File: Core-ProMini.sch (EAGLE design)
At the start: 28 parts, among them CON1 5.08, CON2 2mm, CON3 0.100, IC1 cj7805, J2 IO4, J4 2.1mm, J5 IO4, J6 IO4, J7 IO4

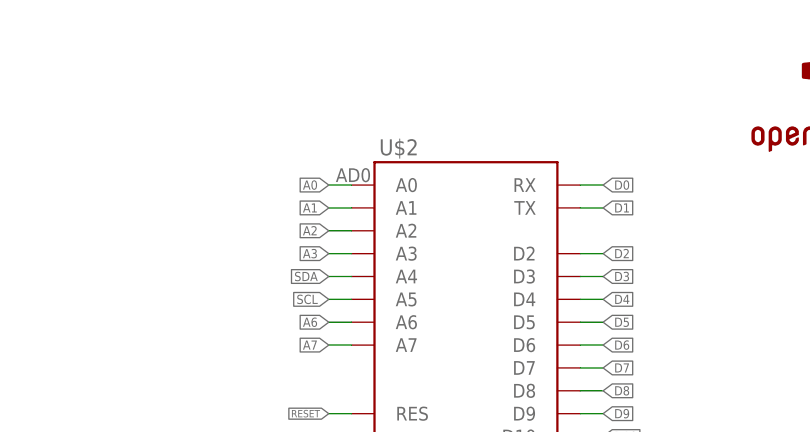
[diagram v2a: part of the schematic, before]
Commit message: updated part names
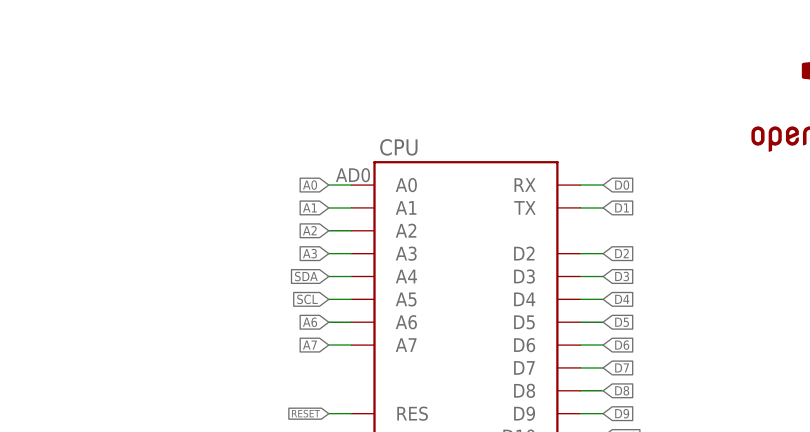
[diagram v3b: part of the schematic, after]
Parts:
- OSH: value DOC-OSHW-LOGO-L -> L
- renumbered LOGO1 to OSH, U$2 to CPU, U$3 to PWR, U$4 to BOARD
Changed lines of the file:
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@@
 <part name="V1" library="supply2" deviceset="GND" device=""/>
 <part name="C5" library="SPCoast" deviceset="CAP-POL*" device="0810" value="150uF"/>
-<part name="U$2" library="SPCoast" deviceset="ARDUINO-PRO-MINI" device="DAVESROBOT"/>
+<part name="CPU" library="SPCoast" deviceset="ARDUINO-PRO-MINI" device="DAVESROBOT"/>
 <part name="J4" library="SPCoast" deviceset="CONNECTOR-DC-POWER" device="-RA" value="2.1mm"/>
-<part name="U$3" library="SPCoast" deviceset="DOC-POWER_LABEL" device="" value="9-12vDC"/>
+<part name="PWR" library="SPCoast" deviceset="DOC-POWER_LABEL" device="" value="9-12vDC"/>
 <part name="VCC12" library="supply1" deviceset="VCCIO" device=""/>
 <part name="V15" library="supply2" deviceset="GND" device=""/>
 <part name="VCC13" library="supply1" deviceset="VCCIO" device=""/>
-<part name="U$4" library="SPCoast" deviceset="BOARD" device="69X100MRCS" value="BOARD69X100MRCS"/>
+<part name="BOARD" library="SPCoast" deviceset="BOARD" device="69X100MRCS" value="BOARD69X100MRCS"/>
 <part name="C1" library="SPCoast" deviceset="CAP*" device="0805" value="1uF"/>
 <part name="C2" library="SPCoast" deviceset="CAP*" device="0805" value="1uF"/>
-<part name="LOGO1" library="SPCoast" deviceset="DOC-OSHW-LOGO-" device="L"/>
+<part name="OSH" library="SPCoast" deviceset="DOC-OSHW-LOGO-" device="L" value="L"/>
 <part name="IC1" library="SPCoast" deviceset="VREG-?-*" device="DPAK" technology="5" value="cj7805"/>
 <part name="CON1" library="SPCoast" deviceset="CONNECTOR-M02" device="508-LOCK" value="5.08"/>
@@
 <instance part="V1" gate="GND" x="160.02" y="68.58" rot="R270"/>
 <instance part="C5" gate="C1" x="175.26" y="96.52"/>
-<instance part="U$2" gate="A" x="190.5" y="144.78"/>
+<instance part="CPU" gate="A" x="190.5" y="144.78"/>
 <instance part="J4" gate="J" x="157.48" y="99.06"/>
-<instance part="U$3" gate="PWR1" x="157.48" y="109.22"/>
+<instance part="PWR" gate="PWR1" x="157.48" y="109.22"/>
 <instance part="VCC12" gate="G$1" x="205.74" y="68.58"/>
 <instance part="V15" gate="GND" x="175.26" y="121.92"/>
 <instance part="VCC13" gate="G$1" x="170.18" y="129.54"/>
-<instance part="U$4" gate="B" x="236.22" y="40.64"/>
+<instance part="BOARD" gate="B" x="236.22" y="40.64"/>
 <instance part="C1" gate="C1" x="203.2" y="96.52" smashed="yes">
 <attribute name="NAME" x="198.501" y="100.076" size="1.778" layer="95" rot="R270"/>
@@
 <attribute name="VALUE" x="184.531" y="95.758" size="1.016" layer="96" rot="R270"/>
 </instance>
-<instance part="LOGO1" gate="DOC-OSHW-LOGO" x="233.68" y="55.88"/>
+<instance part="OSH" gate="DOC-OSHW-LOGO" x="233.68" y="55.88"/>
 <instance part="IC1" gate="VR" x="193.04" y="101.6"/>
 <instance part="CON1" gate="J" x="220.98" y="81.28" rot="MR180"/>
@@
 </segment>
 <segment>
-<pinref part="U$2" gate="A" pin="GND"/>
+<pinref part="CPU" gate="A" pin="GND"/>
 <wire x1="177.8" y1="124.46" x2="175.26" y2="124.46" width="0.1524" layer="91"/>
 <pinref part="V15" gate="GND" pin="GND"/>
@@
 <wire x1="205.74" y1="165.1" x2="203.2" y2="165.1" width="0.1524" layer="91"/>
 <label x="205.74" y="165.1" size="1.016" layer="95" xref="yes"/>
-<pinref part="U$2" gate="A" pin="RX"/>
+<pinref part="CPU" gate="A" pin="RX"/>
 </segment>
 <segment>
@@
 <wire x1="205.74" y1="134.62" x2="203.2" y2="134.62" width="0.1524" layer="91"/>
 <label x="205.74" y="134.62" size="1.016" layer="95" xref="yes"/>
-<pinref part="U$2" gate="A" pin="D11"/>
+<pinref part="CPU" gate="A" pin="D11"/>
 </segment>
 <segment>
@@
 <wire x1="205.74" y1="132.08" x2="203.2" y2="132.08" width="0.1524" layer="91"/>
 <label x="205.74" y="132.08" size="1.016" layer="95" xref="yes"/>
-<pinref part="U$2" gate="A" pin="D12"/>
+<pinref part="CPU" gate="A" pin="D12"/>
 </segment>
 <segment>
@@
 <wire x1="205.74" y1="129.54" x2="203.2" y2="129.54" width="0.1524" layer="91"/>
 <label x="205.74" y="129.54" size="1.016" layer="95" xref="yes"/>
-<pinref part="U$2" gate="A" pin="D13"/>
+<pinref part="CPU" gate="A" pin="D13"/>
 </segment>
 <segment>
@@
 <wire x1="175.26" y1="165.1" x2="177.8" y2="165.1" width="0.1524" layer="91"/>
 <label x="175.26" y="165.1" size="1.016" layer="95" rot="R180" xref="yes"/>
-<pinref part="U$2" gate="A" pin="A0"/>
+<pinref part="CPU" gate="A" pin="A0"/>
 </segment>
 <segment>
@@
 <wire x1="203.2" y1="157.48" x2="205.74" y2="157.48" width="0.1524" layer="91"/>
 <label x="205.74" y="157.48" size="1.016" layer="95" xref="yes"/>
-<pinref part="U$2" gate="A" pin="D2"/>
+<pinref part="CPU" gate="A" pin="D2"/>
 </segment>
 <segment>
@@
 <wire x1="203.2" y1="152.4" x2="205.74" y2="152.4" width="0.1524" layer="91"/>
 <label x="205.74" y="152.4" size="1.016" layer="95" xref="yes"/>
-<pinref part="U$2" gate="A" pin="D4"/>
+<pinref part="CPU" gate="A" pin="D4"/>
 </segment>
 <segment>
@@
 <wire x1="175.26" y1="154.94" x2="177.8" y2="154.94" width="0.1524" layer="91"/>
 <label x="175.26" y="154.94" size="1.016" layer="95" rot="R180" xref="yes"/>
-<pinref part="U$2" gate="A" pin="A4"/>
+<pinref part="CPU" gate="A" pin="A4"/>
 </segment>
 </net>
@@
 <wire x1="175.26" y1="152.4" x2="177.8" y2="152.4" width="0.1524" layer="91"/>
 <label x="175.26" y="152.4" size="1.016" layer="95" rot="R180" xref="yes"/>
-<pinref part="U$2" gate="A" pin="A5"/>
+<pinref part="CPU" gate="A" pin="A5"/>
 </segment>
 </net>
@@
 <wire x1="203.2" y1="142.24" x2="205.74" y2="142.24" width="0.1524" layer="91"/>
 <label x="205.74" y="142.24" size="1.016" layer="95" xref="yes"/>
-<pinref part="U$2" gate="A" pin="D8"/>
+<pinref part="CPU" gate="A" pin="D8"/>
 </segment>
 <segment>
@@
 <wire x1="203.2" y1="144.78" x2="205.74" y2="144.78" width="0.1524" layer="91"/>
 <label x="205.74" y="144.78" size="1.016" layer="95" xref="yes"/>
-<pinref part="U$2" gate="A" pin="D7"/>
+<pinref part="CPU" gate="A" pin="D7"/>
 </segment>
 <segment>
@@
 <wire x1="203.2" y1="154.94" x2="205.74" y2="154.94" width="0.1524" layer="91"/>
 <label x="205.74" y="154.94" size="1.016" layer="95" xref="yes"/>
-<pinref part="U$2" gate="A" pin="D3"/>
+<pinref part="CPU" gate="A" pin="D3"/>
 </segment>
 <segment>
@@
 </segment>
 <segment>
-<pinref part="U$2" gate="A" pin="5V"/>
+<pinref part="CPU" gate="A" pin="5V"/>
 <wire x1="177.8" y1="127" x2="170.18" y2="127" width="0.1524" layer="91"/>
 <pinref part="VCC13" gate="G$1" pin="VCCIO"/>
@@
 <wire x1="205.74" y1="162.56" x2="203.2" y2="162.56" width="0.1524" layer="91"/>
 <label x="205.74" y="162.56" size="1.016" layer="95" xref="yes"/>
-<pinref part="U$2" gate="A" pin="TX"/>
+<pinref part="CPU" gate="A" pin="TX"/>
 </segment>
 <segment>
@@
 <wire x1="205.74" y1="149.86" x2="203.2" y2="149.86" width="0.1524" layer="91"/>
 <label x="205.74" y="149.86" size="1.016" layer="95" xref="yes"/>
-<pinref part="U$2" gate="A" pin="D5"/>
+<pinref part="CPU" gate="A" pin="D5"/>
 </segment>
 <segment>
@@
 <wire x1="205.74" y1="147.32" x2="203.2" y2="147.32" width="0.1524" layer="91"/>
 <label x="205.74" y="147.32" size="1.016" layer="95" xref="yes"/>
-<pinref part="U$2" gate="A" pin="D6"/>
+<pinref part="CPU" gate="A" pin="D6"/>
 </segment>
 <segment>
@@
 <wire x1="205.74" y1="139.7" x2="203.2" y2="139.7" width="0.1524" layer="91"/>
 <label x="205.74" y="139.7" size="1.016" layer="95" xref="yes"/>
-<pinref part="U$2" gate="A" pin="D9"/>
+<pinref part="CPU" gate="A" pin="D9"/>
 </segment>
 <segment>
@@
 <wire x1="205.74" y1="137.16" x2="203.2" y2="137.16" width="0.1524" layer="91"/>
 <label x="205.74" y="137.16" size="1.016" layer="95" xref="yes"/>
-<pinref part="U$2" gate="A" pin="D10"/>
+<pinref part="CPU" gate="A" pin="D10"/>
 </segment>
 <segment>
@@
 <wire x1="175.26" y1="162.56" x2="177.8" y2="162.56" width="0.1524" layer="91"/>
 <label x="175.26" y="162.56" size="1.016" layer="95" rot="R180" xref="yes"/>
-<pinref part="U$2" gate="A" pin="A1"/>
+<pinref part="CPU" gate="A" pin="A1"/>
 </segment>
 <segment>
@@
 <wire x1="175.26" y1="160.02" x2="177.8" y2="160.02" width="0.1524" layer="91"/>
 <label x="175.26" y="160.02" size="1.016" layer="95" rot="R180" xref="yes"/>
-<pinref part="U$2" gate="A" pin="A2"/>
+<pinref part="CPU" gate="A" pin="A2"/>
 </segment>
 <segment>
@@
 <wire x1="175.26" y1="157.48" x2="177.8" y2="157.48" width="0.1524" layer="91"/>
 <label x="175.26" y="157.48" size="1.016" layer="95" rot="R180" xref="yes"/>
-<pinref part="U$2" gate="A" pin="A3"/>
+<pinref part="CPU" gate="A" pin="A3"/>
 </segment>
 <segment>
@@
 <net name="A6" class="0">
 <segment>
-<pinref part="U$2" gate="A" pin="A6"/>
+<pinref part="CPU" gate="A" pin="A6"/>
 <wire x1="177.8" y1="149.86" x2="175.26" y2="149.86" width="0.1524" layer="91"/>
 <label x="175.26" y="149.86" size="1.016" layer="95" rot="R180" xref="yes"/>
@@
 <net name="A7" class="0">
 <segment>
-<pinref part="U$2" gate="A" pin="A7"/>
+<pinref part="CPU" gate="A" pin="A7"/>
 <wire x1="177.8" y1="147.32" x2="175.26" y2="147.32" width="0.1524" layer="91"/>
 <label x="175.26" y="147.32" size="1.016" layer="95" rot="R180" xref="yes"/>
@@
 <net name="RESET" class="0">
 <segment>
-<pinref part="U$2" gate="A" pin="RES"/>
+<pinref part="CPU" gate="A" pin="RES"/>
 <wire x1="177.8" y1="139.7" x2="175.26" y2="139.7" width="0.1524" layer="91"/>
 <label x="175.26" y="139.7" size="0.8128" layer="95" rot="R180" xref="yes"/>

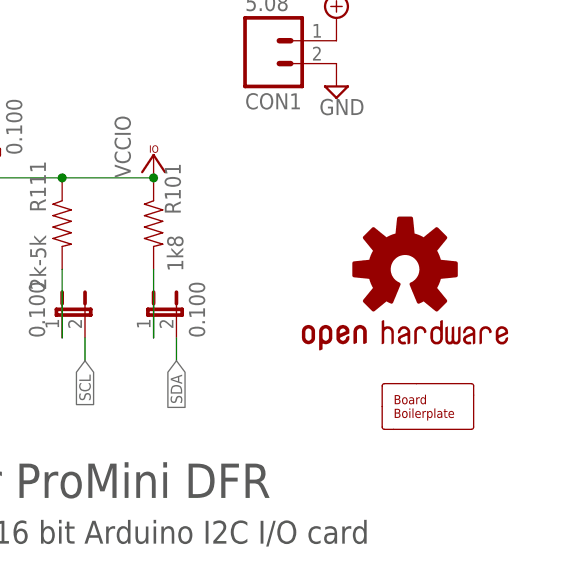
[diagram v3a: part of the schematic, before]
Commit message: updated part names
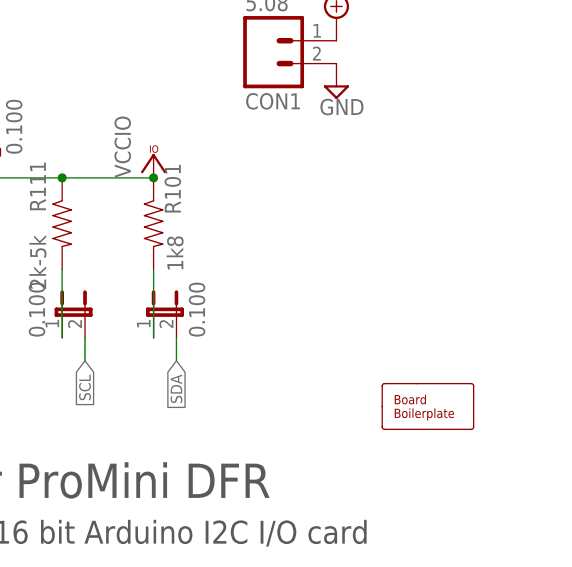
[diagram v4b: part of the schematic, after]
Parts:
- removed U$1: OSHW-LOGOL, SparkFun:OSHW-LOGOL
- OSH: device SPCoast:DOC-OSHW-LOGO-L -> SparkFun:OSHW-LOGOL
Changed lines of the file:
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@@
 <part name="SDA" library="SPCoast" deviceset="JUMPER-2" device="PTH_LOCK" value="0.100"/>
 <part name="SCL" library="SPCoast" deviceset="JUMPER-2" device="PTH_LOCK" value="0.100"/>
-<part name="U$1" library="SparkFun" deviceset="OSHW-LOGO" device="L" value="OSHW-LOGOL"/>
+<part name="OSH" library="SparkFun" deviceset="OSHW-LOGO" device="L" value="L"/>
 <part name="V2" library="supply2" deviceset="GND" device=""/>
 <part name="V3" library="supply2" deviceset="GND" device=""/>
@@
 <part name="C1" library="SPCoast" deviceset="CAP*" device="0805" value="1uF"/>
 <part name="C2" library="SPCoast" deviceset="CAP*" device="0805" value="1uF"/>
-<part name="OSH" library="SPCoast" deviceset="DOC-OSHW-LOGO-" device="L" value="L"/>
 <part name="IC1" library="SPCoast" deviceset="VREG-?-*" device="DPAK" technology="5" value="cj7805"/>
 <part name="CON1" library="SPCoast" deviceset="CONNECTOR-M02" device="508-LOCK" value="5.08"/>
@@
 <attribute name="VALUE" x="193.675" y="48.26" size="1.778" layer="96" rot="R90"/>
 </instance>
-<instance part="U$1" gate="G$1" x="233.68" y="177.8"/>
+<instance part="OSH" gate="G$1" x="233.68" y="177.8"/>
 <instance part="V2" gate="GND" x="83.82" y="48.26"/>
 <instance part="V3" gate="GND" x="83.82" y="83.82"/>
@@
 <attribute name="VALUE" x="184.531" y="95.758" size="1.016" layer="96" rot="R270"/>
 </instance>
-<instance part="OSH" gate="DOC-OSHW-LOGO" x="233.68" y="55.88"/>
 <instance part="IC1" gate="VR" x="193.04" y="101.6"/>
 <instance part="CON1" gate="J" x="220.98" y="81.28" rot="MR180"/>

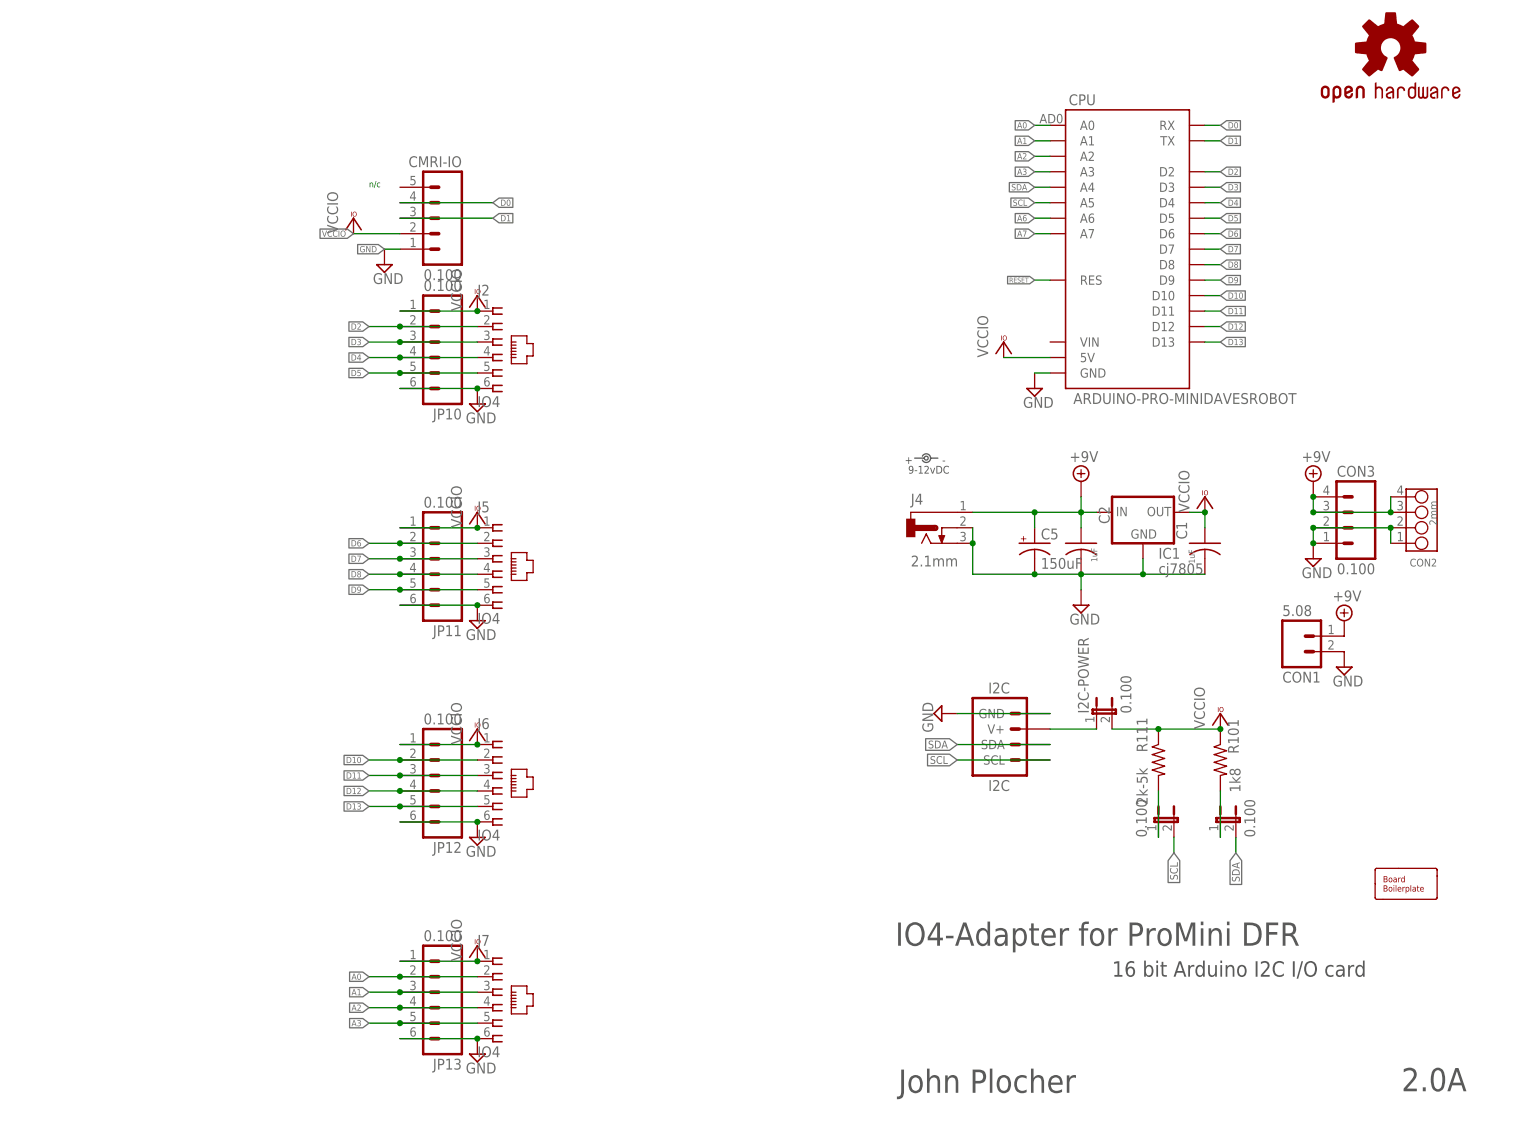
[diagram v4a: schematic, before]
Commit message: normalized values
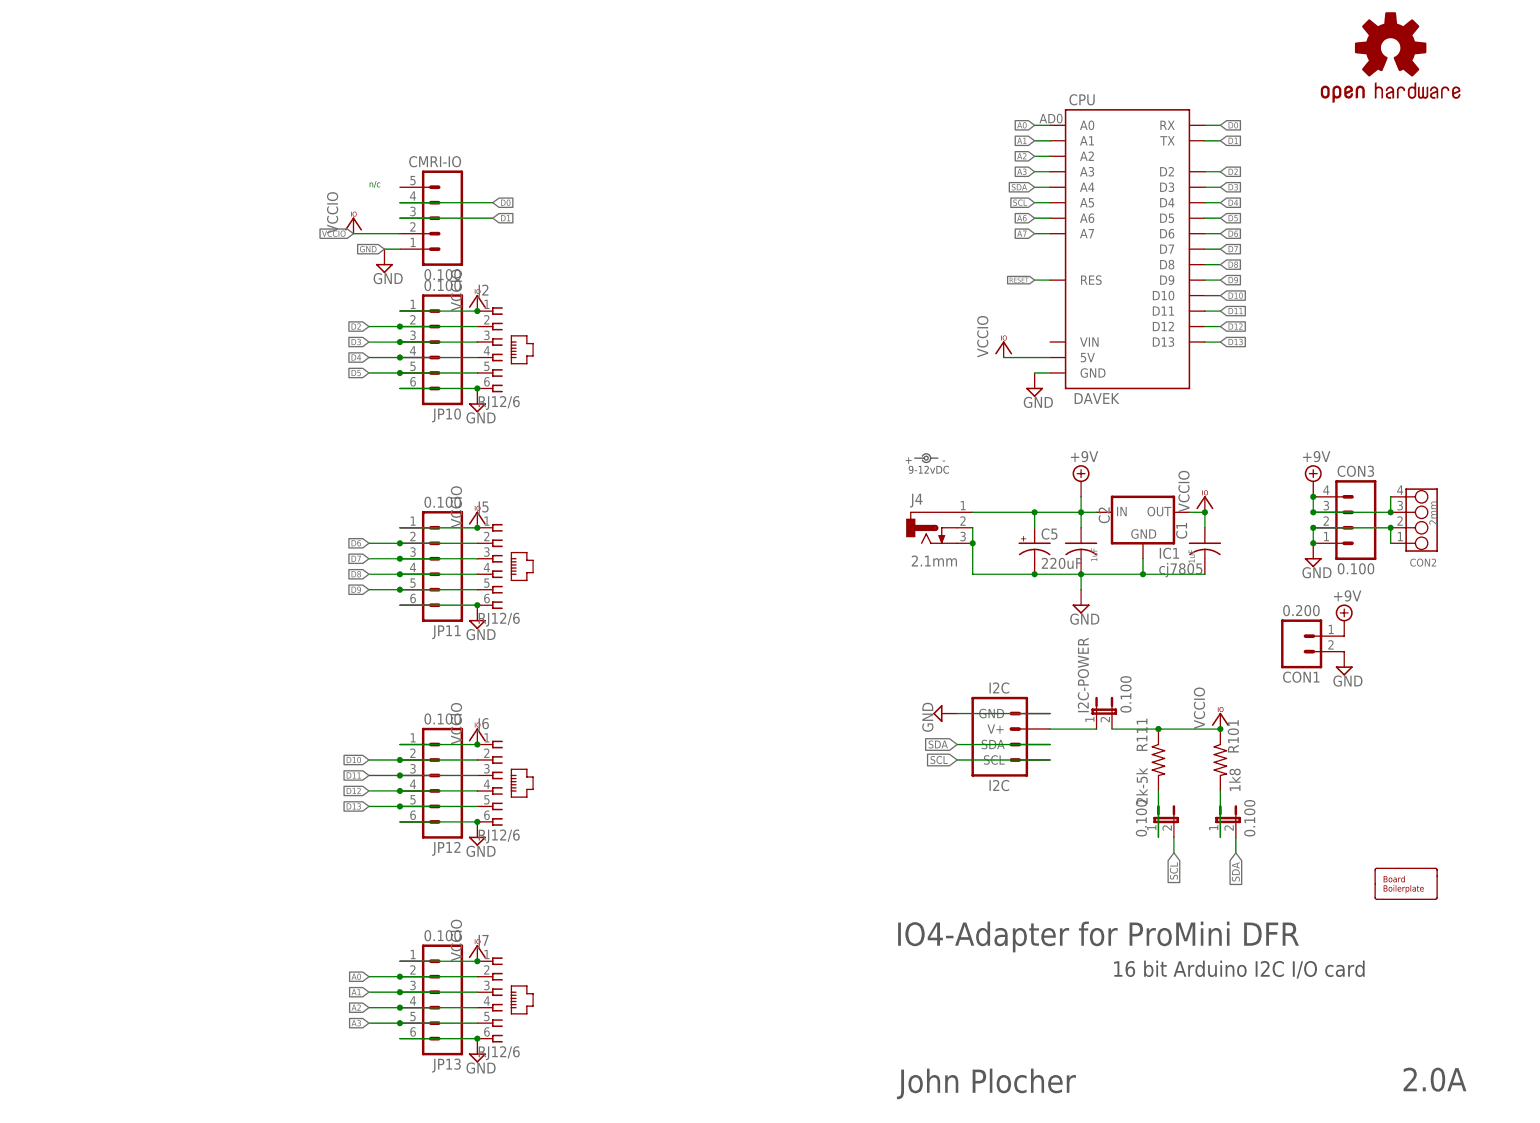
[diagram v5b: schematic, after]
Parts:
- BOARD: value BOARD69X100MRCS -> BOARD; device SPCoast:BOARD69X100MRCS -> SPCoast:BOARD80X100
- C1, C2: device SPCoast:CAP0805 -> SPCoast:CAP0603
- C5: value 150uF -> 220uF
- CON1: value 5.08 -> 0.200
- CPU: value ARDUINO-PRO-MINIDAVESROBOT -> DAVEK
- J2, J5, J6, J7: value IO4 -> RJ12/6
- OSH: value L -> OSHW
- R101, R111: device SPCoast:R0805-RES -> SPCoast:R0603-RES
